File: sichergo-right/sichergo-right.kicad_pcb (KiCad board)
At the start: 2 copper layers, 173 parts, among them J1 Conn_01x04_Pin, J2 Conn_01x04_Pin, Q1 2N7002, Q2 2N7002, SW1 SW_Push, SW10 SW_Push, SW11 SW_Push, SW12 SW_Push, SW13 SW_Push, SW14 SW_Push, SW15 SW_Push, SW16 SW_Push, SW17 SW_Push, SW18 SW_Push, SW19 SW_Push, SW20 SW_Push, SW21 SW_Push, SW22 SW_Push, SW23 SW_Push, SW24 SW_Push, SW25 SW_Push, SW26 SW_Push, SW27 SW_Push, SW28 SW_Push, SW29 SW_Push, SW3 SW_Push, SW30 SW_Push, SW31 SW_Push, SW32 SW_Push, SW33 SW_Push, SW34 SW_Push, SW35 SW_Push, SW36 SW_Push, SW37 SW_Push, SW4 SW_Push, SW5 SW_Push, SW6 SW_Push, SW7 SW_Push, SW8 SW_Push, SW9 SW_Push, U1 AZ1117-3.3, U10 SN74LVC1G125DBV, U2 TPD4E05U06DQA, U3 YTS1C0033BBG01, U4 STM32F103C8Tx, U5 SN74LVC1G125DBV, U6 SN74LVC1G125DBV, U7 YTS1C0033BBG01, U8 STM32F103C8Tx, U9 SN74LVC1G125DBV, Y1 Crystal_GND24, Y2 Crystal_GND24

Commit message: Split design in two PCBs and remake layout
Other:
- board outline added: 268.1 x 155.2 mm

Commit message: Remake entire shape
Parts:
- removed Audio2: PJ-327E-SMT, easyeda2kicad:AUDIO-SMD_PJ-327E-SMT
- removed D38, D39, D40, D41, D42, D43, D44, D45, D46, D47, D48, D49, D50, D51, D52, D53, D54, D55, D56, D57, D58, D59, D60, D61, D62, D63, D64, D65, D66, D67, D68, D69, D70, D71, D72, D73: LED, LED_SMD:LED_0603_1608Metric_Pad1.05x0.95mm_HandSolder
- removed J2: Conn_01x04_Pin, Connector_PinSocket_2.54mm:PinSocket_1x04_P2.54mm_Horizontal
- removed Q2: 2N7002, Package_TO_SOT_SMD:SOT-23_Handsoldering
- removed R29, R30, R32, R33, R34, R35, R36, R37, R38, R39, R40, R41, R42, R43, R44, R45, R46, R47, R48, R49, R50: 1 kohm, Resistor_SMD:R_0603_1608Metric_Pad0.98x0.95mm_HandSolder
- removed R51, R52: 5.1 kohm, Resistor_SMD:R_0612_1632Metric_Pad1.18x3.40mm_HandSolder
- removed SW20, SW21, SW22, SW23, SW24, SW25, SW26, SW27, SW28, SW29, SW30, SW31, SW32, SW33, SW34, SW35, SW36, SW37: SW_Push, personal:Gateron_Milky_Yellow
- removed U10, U9: SN74LVC1G125DBV, Package_TO_SOT_SMD:SOT-23-5_HandSoldering
- removed U7: YTS1C0033BBG01, easyeda2kicad:SW-SMD_YIYUAN_YTS1C003XXX
- removed U8: STM32F103C8Tx, Package_QFP:LQFP-48_7x7mm_P0.5mm
- removed Y2: Crystal_GND24, Crystal:Crystal_SMD_3225-4Pin_3.2x2.5mm_HandSoldering
- added C1: 10 µF, Capacitor_SMD:C_0805_2012Metric_Pad1.18x1.45mm_HandSolder, F.Cu at (138.7, 36.0)
- added C10: 10 µF, Capacitor_SMD:C_0805_2012Metric_Pad1.18x1.45mm_HandSolder, F.Cu at (193.1, 12.2)
- added C11: 0.1 µF, Capacitor_SMD:C_0805_2012Metric_Pad1.18x1.45mm_HandSolder, F.Cu at (168.4, 20.8)
- added C12: 1 µF, Capacitor_SMD:C_0805_2012Metric_Pad1.18x1.45mm_HandSolder, F.Cu at (164.8, 20.8)
- added C13: 10000 pF, Capacitor_SMD:C_0805_2012Metric_Pad1.18x1.45mm_HandSolder, F.Cu at (133.0, 25.6)
- added C2: 22 µF, Capacitor_SMD:C_0805_2012Metric_Pad1.18x1.45mm_HandSolder, F.Cu at (115.0, 20.8)
- added C3: 10 pF, Capacitor_SMD:C_0805_2012Metric_Pad1.18x1.45mm_HandSolder, F.Cu at (173.4, 26.4)
- added C4: 10 pF, Capacitor_SMD:C_0805_2012Metric_Pad1.18x1.45mm_HandSolder, F.Cu at (170.4, 20.8)
- added C5: 0.1 µF, Capacitor_SMD:C_0805_2012Metric_Pad1.18x1.45mm_HandSolder, F.Cu at (162.8, 20.8)
- added C6: 0.1 µF, Capacitor_SMD:C_0805_2012Metric_Pad1.18x1.45mm_HandSolder, F.Cu at (165.3, 29.5)
- added C7: 0.1 µF, Capacitor_SMD:C_0805_2012Metric_Pad1.18x1.45mm_HandSolder, F.Cu at (151.5, 20.1)
- added C8: 0.1 µF, Capacitor_SMD:C_0805_2012Metric_Pad1.18x1.45mm_HandSolder, F.Cu at (148.4, 36.4)
- added C9: 0.1 µF, Capacitor_SMD:C_0805_2012Metric_Pad1.18x1.45mm_HandSolder, F.Cu at (193.1, 10.1)
- added L1: 120 Ohm @ 100 MHz, Inductor_SMD:L_0603_1608Metric_Pad1.05x0.95mm_HandSolder, F.Cu at (122.9, 19.5)
- added R10: 1 kohm, Resistor_SMD:R_0603_1608Metric_Pad0.98x0.95mm_HandSolder, F.Cu at (98.5, 88.6)
- added R11: 1 kohm, Resistor_SMD:R_0603_1608Metric_Pad0.98x0.95mm_HandSolder, F.Cu at (98.6, 108.1)
- added R12: 1 kohm, Resistor_SMD:R_0603_1608Metric_Pad0.98x0.95mm_HandSolder, F.Cu at (95.0, 67.0)
- added R3: 4.7 kohm, Resistor_SMD:R_0603_1608Metric_Pad0.98x0.95mm_HandSolder, F.Cu at (133.5, 20.9)
- added R4: 4.7 kohm, Resistor_SMD:R_0603_1608Metric_Pad0.98x0.95mm_HandSolder, F.Cu at (200.2, 52.5)
- added R5: 4.7 kohm, Resistor_SMD:R_0603_1608Metric_Pad0.98x0.95mm_HandSolder, F.Cu at (207.0, 51.9)
- added R6: 4.7 kohm, Resistor_SMD:R_0603_1608Metric_Pad0.98x0.95mm_HandSolder, F.Cu at (165.5, 49.3)
- added R9: 100 ohm, Resistor_SMD:R_0603_1608Metric_Pad0.98x0.95mm_HandSolder, F.Cu at (197.9, 17.1)
- added SW2: SW_Push, personal:Gateron_Milky_Yellow, F.Cu at (100.3, 78.9)
- added TP1: TestPoint, TestPoint:TestPoint_THTPad_1.0x1.0mm_Drill0.5mm, F.Cu at (116.0, 18.5)
- added TP3: TestPoint, TestPoint:TestPoint_THTPad_1.0x1.0mm_Drill0.5mm, F.Cu at (119.4, 25.4)
- added TP4: TestPoint, TestPoint:TestPoint_THTPad_1.0x1.0mm_Drill0.5mm, F.Cu at (105.9, 28.5)
- added TP7: TestPoint, TestPoint:TestPoint_THTPad_1.0x1.0mm_Drill0.5mm, F.Cu at (93.5, 33.0)
- added TP8: TestPoint, TestPoint:TestPoint_THTPad_1.0x1.0mm_Drill0.5mm, F.Cu at (200.2, 11.3)
- added TP9: TestPoint, TestPoint:TestPoint_THTPad_1.0x1.0mm_Drill0.5mm, F.Cu at (197.8, 11.2)
- D10, D14, D15, D16, D17, D2, D22, D23, D24, D25, D3, D30, D31, D32, D33, D4, D8, D9: value CD4148W -> LED; footprint Diode_SMD:D_0805_2012Metric_Pad1.15x1.40mm_HandSolder -> LED_SMD:LED_0603_1608Metric_Pad1.05x0.95mm_HandSolder
- R13: value 5.1 kohm -> 1 kohm
- R14: value 100 ohm -> 1 kohm; footprint Resistor_SMD:R_0805_2012Metric_Pad1.20x1.40mm_HandSolder -> Resistor_SMD:R_0603_1608Metric_Pad0.98x0.95mm_HandSolder
- R2, R8: value 4.7 kohm -> 5.1 kohm
- R28: value 1 kohm -> 4.7 kohm
- R31: value 1 kohm -> 1.5 kohm
- R7: value 100 ohm -> 4.7 kohm; footprint Resistor_SMD:R_0805_2012Metric_Pad1.20x1.40mm_HandSolder -> Resistor_SMD:R_0603_1608Metric_Pad0.98x0.95mm_HandSolder
- SW19: value SW_Push -> MS-22C01-G010; footprint personal:Gateron_Milky_Yellow -> easyeda2kicad:SW-SMD_6P-L7.2-W3.5-P2.50-LS6.0-TL
- moved D21 253.1 mm to (137.0, 126.8), turned to 90 degrees
- moved D17 253.0 mm to (129.9, 127.7), turned to 180 degrees
- moved D37 251.1 mm to (180.0, 132.7), turned to 90 degrees
- moved D29 249.9 mm to (157.5, 130.2), turned to 90 degrees
- moved D3 249.6 mm to (102.3, 108.1), turned to 180 degrees
- moved D10 243.9 mm to (116.9, 106.0), turned to 180 degrees
- moved D16 243.3 mm to (132.1, 105.9), turned to 180 degrees
- moved D33 241.3 mm to (170.9, 132.5), turned to 150 degrees
- moved D25 240.7 mm to (149.1, 130.4), turned to 165 degrees
- moved D20 236.1 mm to (136.3, 105.8), turned to 90 degrees
- moved D2 234.5 mm to (102.1, 88.6), turned to 180 degrees
- moved D13 233.8 mm to (121.0, 105.8), turned to 90 degrees
- moved D7 230.3 mm to (109.9, 102.6), turned to 90 degrees
- moved D28 229.5 mm to (151.2, 107.1), turned to 90 degrees
- moved D9 229.0 mm to (117.0, 86.9), turned to 180 degrees
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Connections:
- D1 pad 2: /KBD_L/VBUS -> (no net)
- D10 pad 1: /KBD_L/KB_ROW_1 -> GND
- D11 pad 1: /KBD_L/KB_ROW_1 -> (no net)
- D12 pad 1: /KBD_L/KB_ROW_2 -> (no net)
- D13 pad 1: /KBD_L/KB_ROW_2 -> (no net)
- D14 pad 1: /KBD_L/KB_ROW_2 -> GND
- D15 pad 1: /KBD_L/KB_ROW_2 -> GND
- D16 pad 1: /KBD_L/KB_ROW_2 -> GND
- D17 pad 1: /KBD_R/KB_ROW_4 -> GND
- D18 pad 1: /KBD_R/KB_ROW_5 -> (no net)
- D19 pad 1: /KBD_L/KB_ROW_3 -> (no net)
- D2 pad 1: /KBD_L/KB_ROW_0 -> GND
- D20 pad 1: /KBD_L/KB_ROW_3 -> (no net)
- D21 pad 1: /KBD_L/KB_ROW_3 -> (no net)
- D22 pad 1: /KBD_R/KB_ROW_6 -> GND
- D23 pad 1: /KBD_R/KB_ROW_4 -> GND
- D24 pad 1: /KBD_R/KB_ROW_5 -> GND
- D25 pad 1: /KBD_R/KB_ROW_6 -> GND
- D26 pad 1: /KBD_R/KB_ROW_4 -> (no net)
- D27 pad 1: /KBD_R/KB_ROW_5 -> (no net)
- D28 pad 1: /KBD_R/KB_ROW_6 -> (no net)
- D29 pad 1: /KBD_R/KB_ROW_7 -> (no net)
- D3 pad 1: /KBD_L/KB_ROW_0 -> GND
- D30 pad 1: /KBD_R/KB_ROW_4 -> GND
- D31 pad 1: /KBD_R/KB_ROW_5 -> GND
- D32 pad 1: /KBD_R/KB_ROW_6 -> GND
- D33 pad 1: /KBD_R/KB_ROW_7 -> GND
- D34 pad 1: /KBD_R/KB_ROW_4 -> (no net)
- D35 pad 1: /KBD_R/KB_ROW_5 -> (no net)
- D36 pad 1: /KBD_R/KB_ROW_6 -> (no net)
- D37 pad 1: /KBD_R/KB_ROW_7 -> (no net)
- D4 pad 1: /KBD_L/KB_ROW_0 -> GND
- D5 pad 1: /KBD_L/KB_ROW_0 -> (no net)
- D6 pad 1: /KBD_L/KB_ROW_0 -> (no net)
- D7 pad 1: /KBD_L/KB_ROW_1 -> (no net)
- D8 pad 1: /KBD_L/KB_ROW_1 -> GND
- D9 pad 1: /KBD_L/KB_ROW_1 -> GND
- F1 pad 1: /KBD_L/VBUS -> (no net)
- Q1 pad 3: +3V3 -> (no net)
- R1 pad 1: Net-(USB1-CC1) -> Net-(USB1-CC2)
- R13 pad 1: Net-(USB1-CC2) -> (no net)
- R13 pad 2: GND -> Net-(D8-A)
- R14 pad 1: Net-(Audio2-Pad1) -> (no net)
- R14 pad 2: GND -> Net-(D9-A)
- R15 pad 1: +3V3 -> (no net)
- R15 pad 2: Net-(D38-A) -> Net-(D10-A)
- R16 pad 1: +3V3 -> (no net)
- R16 pad 2: Net-(D39-A) -> Net-(D14-A)
- R17 pad 1: +3V3 -> (no net)
- R17 pad 2: Net-(D40-A) -> Net-(D15-A)
- R18 pad 1: +3V3 -> (no net)
- R18 pad 2: Net-(D44-A) -> Net-(D16-A)
- R19 pad 1: +3V3 -> (no net)
- R19 pad 2: Net-(D45-A) -> Net-(D17-A)
- R2 pad 1: +3V3 -> Net-(USB1-CC1)
- R2 pad 2: Net-(U4-NRST) -> GND
- R20 pad 1: +3V3 -> (no net)
- R20 pad 2: Net-(D43-A) -> Net-(D22-A)
- R21 pad 1: +3V3 -> (no net)
- R21 pad 2: Net-(D48-A) -> Net-(D23-A)
- R22 pad 1: +3V3 -> (no net)
- R22 pad 2: Net-(D42-A) -> Net-(D24-A)
- R23 pad 1: +3V3 -> (no net)
- R23 pad 2: Net-(D41-A) -> Net-(D25-A)
- R24 pad 1: +3V3 -> (no net)
- R24 pad 2: Net-(D51-A) -> Net-(D30-A)
- R25 pad 1: +3V3 -> (no net)
- R25 pad 2: Net-(D50-A) -> Net-(D31-A)
- R26 pad 1: +3V3 -> (no net)
- R26 pad 2: Net-(D49-A) -> Net-(D32-A)
- R27 pad 1: +3V3 -> (no net)
- R27 pad 2: Net-(D46-A) -> Net-(D33-A)
- R28 pad 1: +3V3 -> (no net)
- R28 pad 2: Net-(D47-A) -> +3V3
- R31 pad 2: Net-(D53-A) -> (no net)
- R7 pad 1: Net-(Audio1-Pad1) -> Net-(U4-BOOT0)
- R8 pad 1: +3V3 -> Net-(Q1-G)
- R8 pad 2: Net-(U8-NRST) -> GND
- SW1 pad 1: /KBD_L/KB_COL_0 -> (no net)
- SW1 pad 2: Net-(D2-A) -> Net-(D5-A)
- SW10 pad 1: /KBD_L/KB_COL_3 -> (no net)
- SW10 pad 2: Net-(D10-A) -> Net-(D21-A)
- SW11 pad 1: /KBD_L/KB_COL_4 -> (no net)
- SW11 pad 2: Net-(D11-A) -> Net-(D26-A)
- SW12 pad 1: /KBD_L/KB_COL_0 -> (no net)
- SW12 pad 2: Net-(D12-A) -> Net-(D27-A)
- SW13 pad 1: /KBD_L/KB_COL_1 -> (no net)
- SW13 pad 2: Net-(D13-A) -> Net-(D28-A)
- SW14 pad 1: /KBD_L/KB_COL_2 -> (no net)
- SW14 pad 2: Net-(D14-A) -> Net-(D29-A)
- SW15 pad 1: /KBD_L/KB_COL_3 -> (no net)
- SW15 pad 2: Net-(D15-A) -> Net-(D34-A)
- SW16 pad 1: /KBD_L/KB_COL_4 -> (no net)
- SW16 pad 2: Net-(D16-A) -> Net-(D35-A)
- SW17 pad 1: /KBD_R/KB_COL_0 -> (no net)
- SW17 pad 2: Net-(D17-A) -> Net-(D36-A)
- SW18 pad 1: /KBD_R/KB_COL_0 -> (no net)
- SW18 pad 2: Net-(D18-A) -> Net-(D37-A)
- SW19 pad 1: /KBD_L/KB_COL_2 -> (no net)
- SW19 pad 2: Net-(D19-A) -> Net-(J1-Pin_3)
- SW3 pad 1: /KBD_L/KB_COL_1 -> (no net)
- SW3 pad 2: Net-(D3-A) -> Net-(D7-A)
- SW4 pad 1: /KBD_L/KB_COL_2 -> (no net)
- SW4 pad 2: Net-(D4-A) -> Net-(D11-A)
- SW5 pad 1: /KBD_L/KB_COL_3 -> (no net)
- SW5 pad 2: Net-(D5-A) -> Net-(D12-A)
- SW6 pad 1: /KBD_L/KB_COL_4 -> (no net)
- SW6 pad 2: Net-(D6-A) -> Net-(D13-A)
- SW7 pad 1: /KBD_L/KB_COL_0 -> (no net)
- SW7 pad 2: Net-(D7-A) -> Net-(D18-A)
- SW8 pad 1: /KBD_L/KB_COL_1 -> (no net)
- SW8 pad 2: Net-(D8-A) -> Net-(D19-A)
- SW9 pad 1: /KBD_L/KB_COL_2 -> (no net)
- SW9 pad 2: Net-(D9-A) -> Net-(D20-A)
- U2 pad 1: /KBD_L/D+ -> (no net)
- U2 pad 2: /KBD_L/D- -> (no net)
- U4 pad 10: /KBD_L/KB_COL_0 -> (no net)
- U4 pad 11: /KBD_L/KB_COL_1 -> (no net)
- U4 pad 12: /KBD_L/KB_COL_2 -> (no net)
- U4 pad 13: /KBD_L/KB_COL_3 -> (no net)
- U4 pad 14: /KBD_L/KB_COL_4 -> (no net)
- U4 pad 15: /KBD_L/KB_ROW_0 -> (no net)
- U4 pad 16: /KBD_L/KB_ROW_1 -> (no net)
- U4 pad 17: /KBD_L/KB_ROW_2 -> (no net)
- U4 pad 26: Net-(Q2-G) -> Net-(Q1-G)
- U4 pad 29: /KBD_L/KB_ROW_3 -> (no net)
- U4 pad 30: /KBD_L/UART_TX -> (no net)
- U4 pad 31: /KBD_L/UART_RX -> (no net)
- U4 pad 32: unconnected-(U4-PA11-Pad32) -> (no net)
- U4 pad 33: unconnected-(U4-PA12-Pad33) -> (no net)
- U4 pad 34: /KBD_L/SWDIO -> (no net)
- U4 pad 37: /KBD_L/SWCLK -> (no net)
- U4 pad 38: unconnected-(U4-PA15-Pad38) -> (no net)
- U4 pad 39: unconnected-(U4-PB3-Pad39) -> (no net)
- U4 pad 40: unconnected-(U4-PB4-Pad40) -> (no net)
- U4 pad 41: unconnected-(U4-PB5-Pad41) -> (no net)
- U4 pad 42: /KBD_L/OLED_SCL -> (no net)
- U4 pad 43: /KBD_L/OLED_SDA -> (no net)
- U5 pad 2: /KBD_L/UART_TX -> Net-(Audio1-Pad4)
- U5 pad 4: Net-(Audio1-Pad3) -> (no net)
- U6 pad 2: Net-(Audio1-Pad4) -> (no net)
- U6 pad 4: /KBD_L/UART_RX -> Net-(Audio1-Pad3)
- USB1 pad 11: /KBD_L/VBUS -> (no net)
- USB1 pad 13: GND -> (no net)
- USB1 pad 14: GND -> (no net)
- USB1 pad 2: /KBD_L/VBUS -> (no net)
- USB1 pad 5: /KBD_L/D- -> (no net)
- USB1 pad 6: /KBD_L/D+ -> (no net)
- USB1 pad 7: /KBD_L/D- -> (no net)
- USB1 pad 8: /KBD_L/D+ -> (no net)
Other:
- board outline removed
- board text added: "Daniel (steewBSD)"
- board text added: "NP"

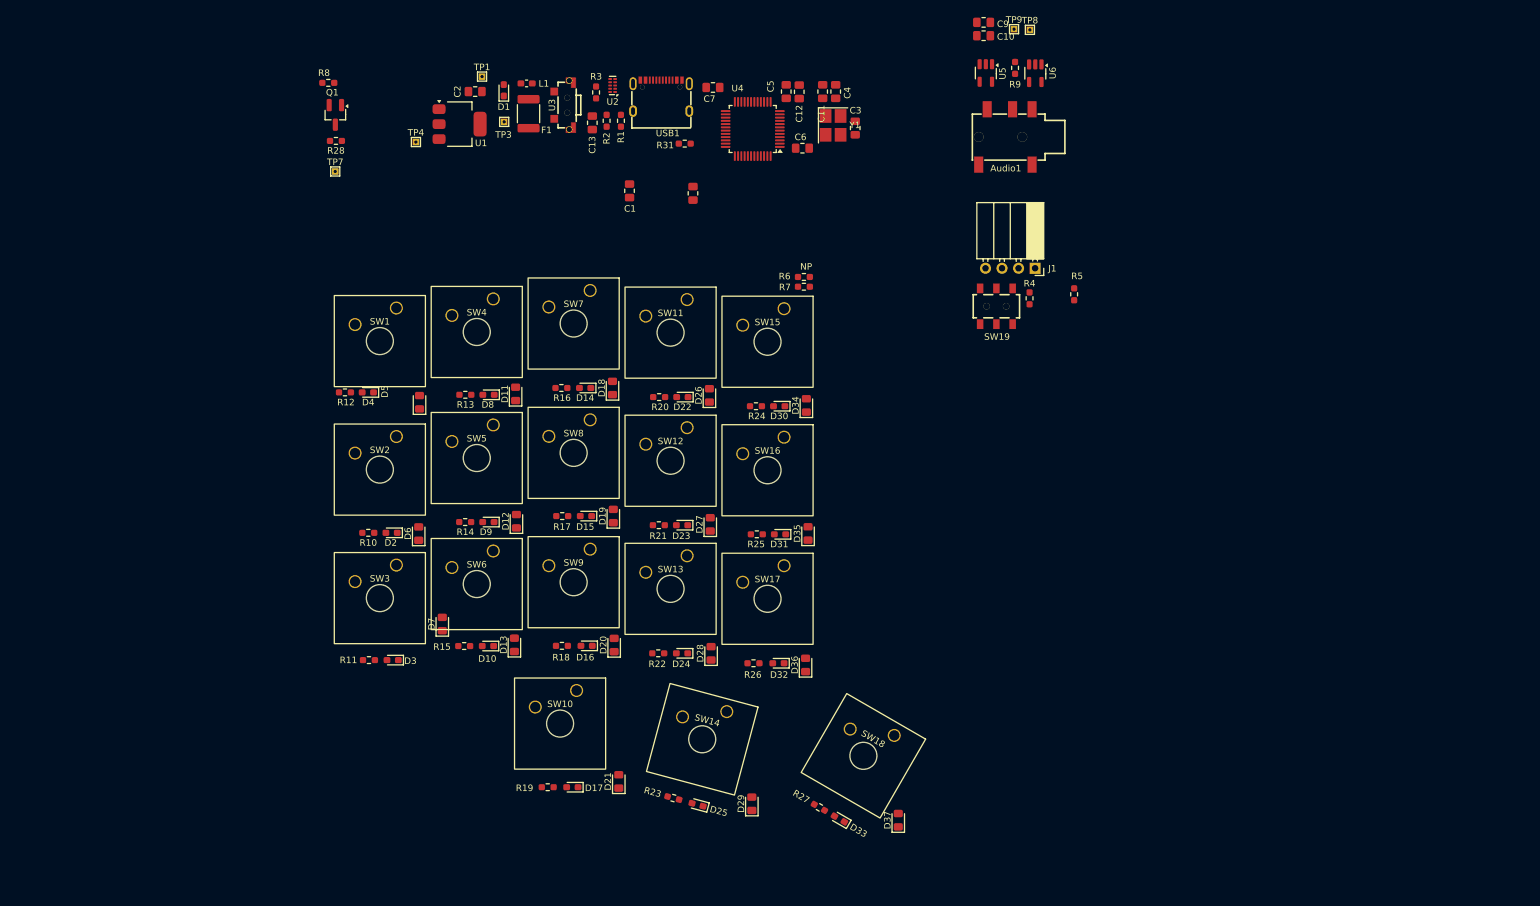
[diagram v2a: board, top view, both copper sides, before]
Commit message: Fix keyboard layout size
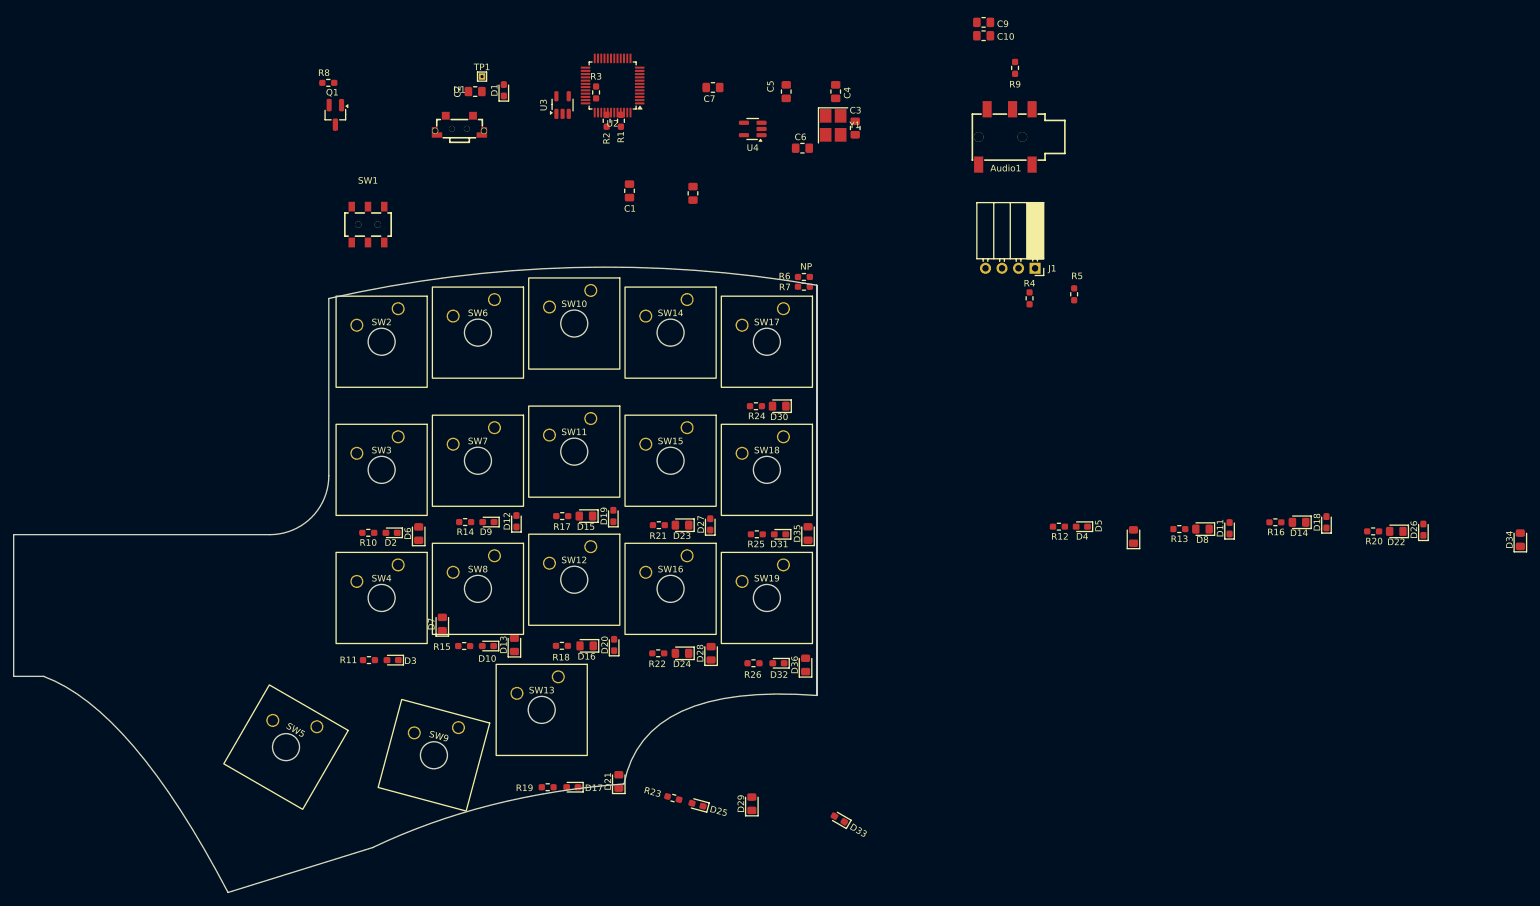
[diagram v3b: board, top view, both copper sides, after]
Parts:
- removed C11: 0.1 µF, Capacitor_SMD:C_0805_2012Metric_Pad1.18x1.45mm_HandSolder
- removed C12: 1 µF, Capacitor_SMD:C_0805_2012Metric_Pad1.18x1.45mm_HandSolder
- removed C13: 10000 pF, Capacitor_SMD:C_0805_2012Metric_Pad1.18x1.45mm_HandSolder
- removed D37: CD4148W, Diode_SMD:D_0805_2012Metric_Pad1.15x1.40mm_HandSolder
- removed F1: 1812L050/30PR, Fuse:Fuse_1812_4532Metric_Pad1.30x3.40mm_HandSolder
- removed L1: 120 Ohm @ 100 MHz, Inductor_SMD:L_0603_1608Metric_Pad1.05x0.95mm_HandSolder
- removed R27: 1 kohm, Resistor_SMD:R_0603_1608Metric_Pad0.98x0.95mm_HandSolder
- removed R28: 4.7 kohm, Resistor_SMD:R_0603_1608Metric_Pad0.98x0.95mm_HandSolder
- removed R31: 1.5 kohm, Resistor_SMD:R_0603_1608Metric_Pad0.98x0.95mm_HandSolder
- removed TP3, TP4, TP7, TP8, TP9: TestPoint, TestPoint:TestPoint_THTPad_1.0x1.0mm_Drill0.5mm
- removed U5, U6: SN74LVC1G125DBV, Package_TO_SOT_SMD:SOT-23-5_HandSoldering
- removed USB1: TYPE-C 16PIN 2MD(073), easyeda2kicad:USB-C-SMD_TYPE-C-6PIN-2MD-073
- C1: value 10 µF -> 10 pF
- C10: value 10 µF -> 1 µF
- C2: value 22 µF -> 10 pF
- C3, C4: value 10 pF -> 0.1 µF
- C8: value 0.1 µF -> 10 µF
- D1: value CPDUR5V0HE-HF -> LED; footprint Diode_SMD:D_0603_1608Metric_Pad1.05x0.95mm_HandSolder -> LED_SMD:LED_0603_1608Metric_Pad1.05x0.95mm_HandSolder
- D11, D12, D18, D19, D20, D26, D27: value CD4148W -> LED; footprint Diode_SMD:D_0805_2012Metric_Pad1.15x1.40mm_HandSolder -> LED_SMD:LED_0603_1608Metric_Pad1.05x0.95mm_HandSolder
- D14, D15, D16, D22, D23, D24, D30, D8: value LED -> CD4148W; footprint LED_SMD:LED_0603_1608Metric_Pad1.05x0.95mm_HandSolder -> Diode_SMD:D_0805_2012Metric_Pad1.15x1.40mm_HandSolder
- R1, R2: value 5.1 kohm -> 4.7 kohm
- R7: value 4.7 kohm -> 5.1 kohm
- R8: value 5.1 kohm -> 100 ohm
- R9: value 100 ohm -> 1 kohm
- SW1: value SW_Push -> MS-22C01-G010; footprint personal:Gateron_Milky_Yellow -> easyeda2kicad:SW-SMD_6P-L7.2-W3.5-P2.50-LS6.0-TL
- SW19: value MS-22C01-G010 -> SW_Push; footprint easyeda2kicad:SW-SMD_6P-L7.2-W3.5-P2.50-LS6.0-TL -> personal:Gateron_Milky_Yellow
- U1: value AZ1117-3.3 -> YTS1C0033BBG01; footprint Package_TO_SOT_SMD:SOT-223-3_TabPin2 -> easyeda2kicad:SW-SMD_YIYUAN_YTS1C003XXX
- U2: value TPD4E05U06DQA -> STM32F103C8Tx; footprint Package_SON:USON-10_2.5x1.0mm_P0.5mm -> Package_QFP:LQFP-48_7x7mm_P0.5mm
- U3: value YTS1C0033BBG01 -> SN74LVC1G125DBV; footprint easyeda2kicad:SW-SMD_YIYUAN_YTS1C003XXX -> Package_TO_SOT_SMD:SOT-23-5_HandSoldering
- U4: value STM32F103C8Tx -> SN74LVC1G125DBV; footprint Package_QFP:LQFP-48_7x7mm_P0.5mm -> Package_TO_SOT_SMD:SOT-23-5_HandSoldering
- moved D8 111.6 mm to (226.7, 88.0)
- moved R12 111.6 mm to (204.7, 87.6)
- moved D11 111.6 mm to (230.9, 87.9)
- moved D14 111.6 mm to (241.6, 87.0)
- moved D18 111.6 mm to (245.8, 87.0)
- moved D26 111.6 mm to (260.7, 88.1)
- moved D34 111.6 mm to (275.6, 89.6)
- moved D4 111.6 mm to (208.2, 87.6)
- moved D5 111.6 mm to (216.1, 89.1)
- moved R13 111.6 mm to (223.2, 88.0)
- moved R16 111.6 mm to (237.9, 87.0)
- moved R20 111.6 mm to (253.0, 88.4)
- moved D22 111.6 mm to (256.5, 88.4)
- moved SW14 62.7 mm to (145.0, 57.8), turned to 0 degrees
- moved SW10 61.5 mm to (130.2, 56.4)
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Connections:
- C1 pad 1: (no net) -> Net-(U2-PD0)
- C2 pad 1: +3V3 -> Net-(U2-PD1)
- C3 pad 1: Net-(U4-PD0) -> Net-(U2-NRST)
- C4 pad 1: Net-(U4-PD1) -> +3V3
- C5 pad 1: Net-(U4-NRST) -> +3V3
- D1 pad 2: (no net) -> Net-(D1-A)
- D11 pad 1: (no net) -> GND
- D12 pad 1: (no net) -> GND
- D13 pad 1: (no net) -> /KB_ROW_0
- D14 pad 1: GND -> /KB_ROW_1
- D15 pad 1: GND -> /KB_ROW_2
- D16 pad 1: GND -> /KB_ROW_3
- D18 pad 1: (no net) -> GND
- D19 pad 1: (no net) -> GND
- D20 pad 1: (no net) -> GND
- D21 pad 1: (no net) -> /KB_ROW_0
- D22 pad 1: GND -> /KB_ROW_1
- D23 pad 1: GND -> /KB_ROW_2
- D24 pad 1: GND -> /KB_ROW_3
- D26 pad 1: (no net) -> GND
- D27 pad 1: (no net) -> GND
- D28 pad 1: (no net) -> /KB_ROW_0
- D29 pad 1: (no net) -> /KB_ROW_1
- D30 pad 1: GND -> /KB_ROW_2
- D34 pad 1: (no net) -> /KB_ROW_0
- D35 pad 1: (no net) -> /KB_ROW_1
- D36 pad 1: (no net) -> /KB_ROW_2
- D5 pad 1: (no net) -> /KB_ROW_0
- D6 pad 1: (no net) -> /KB_ROW_1
- D7 pad 1: (no net) -> /KB_ROW_2
- D8 pad 1: GND -> /KB_ROW_3
- Q1 pad 3: (no net) -> /MatrixR/LED_DRIVE
- R1 pad 1: Net-(USB1-CC2) -> +3V3
- R1 pad 2: GND -> /OLED_SCL
- R10 pad 1: (no net) -> /MatrixR/LED_DRIVE
- R11 pad 1: (no net) -> /MatrixR/LED_DRIVE
- R12 pad 1: (no net) -> /MatrixR/LED_DRIVE
- R13 pad 1: (no net) -> /MatrixR/LED_DRIVE
- R13 pad 2: Net-(D8-A) -> Net-(D9-A)
- R14 pad 1: (no net) -> /MatrixR/LED_DRIVE
- R14 pad 2: Net-(D9-A) -> Net-(D10-A)
- R15 pad 1: (no net) -> /MatrixR/LED_DRIVE
- R15 pad 2: Net-(D10-A) -> Net-(D11-A)
- R16 pad 1: (no net) -> /MatrixR/LED_DRIVE
- R16 pad 2: Net-(D14-A) -> Net-(D12-A)
- R17 pad 1: (no net) -> /MatrixR/LED_DRIVE
- R17 pad 2: Net-(D15-A) -> Net-(D17-A)
- R18 pad 1: (no net) -> /MatrixR/LED_DRIVE
- R18 pad 2: Net-(D16-A) -> Net-(D18-A)
- R19 pad 1: (no net) -> /MatrixR/LED_DRIVE
- R19 pad 2: Net-(D17-A) -> Net-(D19-A)
- R2 pad 1: Net-(USB1-CC1) -> +3V3
- R2 pad 2: GND -> Net-(U2-NRST)
- R20 pad 1: (no net) -> /MatrixR/LED_DRIVE
- R20 pad 2: Net-(D22-A) -> Net-(D20-A)
- R21 pad 1: (no net) -> /MatrixR/LED_DRIVE
- R21 pad 2: Net-(D23-A) -> Net-(D25-A)
- R22 pad 1: (no net) -> /MatrixR/LED_DRIVE
- R22 pad 2: Net-(D24-A) -> Net-(D26-A)
- R23 pad 1: (no net) -> /MatrixR/LED_DRIVE
- R23 pad 2: Net-(D25-A) -> Net-(D27-A)
- R24 pad 1: (no net) -> /MatrixR/LED_DRIVE
- R24 pad 2: Net-(D30-A) -> Net-(D31-A)
- R25 pad 1: (no net) -> /MatrixR/LED_DRIVE
- R25 pad 2: Net-(D31-A) -> Net-(D32-A)
- R26 pad 1: (no net) -> /MatrixR/LED_DRIVE
- R26 pad 2: Net-(D32-A) -> Net-(D33-A)
- R3 pad 2: Net-(U4-NRST) -> /OLED_SDA
- R4 pad 2: (no net) -> /MatrixR/LED_DRIVE
- R5 pad 2: (no net) -> Net-(U2-BOOT0)
- R6 pad 1: +3V3 -> Net-(U2-BOOT0)
- R6 pad 2: Net-(U4-BOOT0) -> GND
- R7 pad 1: Net-(U4-BOOT0) -> Net-(Q1-G)
- R8 pad 1: Net-(Q1-G) -> GND
- R8 pad 2: GND -> Net-(Audio1-Pad1)
- R9 pad 1: GND -> /MatrixR/LED_DRIVE
- R9 pad 2: Net-(Audio1-Pad1) -> Net-(D1-A)
- SW1 pad 1: (no net) -> /SWCLK
- SW1 pad 2: Net-(D5-A) -> Net-(J1-Pin_3)
- SW10 pad 1: (no net) -> /KB_COL_2
- SW11 pad 1: (no net) -> /KB_COL_2
- SW11 pad 2: Net-(D26-A) -> Net-(D22-A)
- SW12 pad 1: (no net) -> /KB_COL_2
- SW12 pad 2: Net-(D27-A) -> Net-(D23-A)
- SW13 pad 1: (no net) -> /KB_COL_2
- SW13 pad 2: Net-(D28-A) -> Net-(D24-A)
- SW14 pad 1: (no net) -> /KB_COL_3
- SW14 pad 2: Net-(D29-A) -> Net-(D28-A)
- SW15 pad 1: (no net) -> /KB_COL_3
- SW15 pad 2: Net-(D34-A) -> Net-(D29-A)
- SW16 pad 1: (no net) -> /KB_COL_3
- SW16 pad 2: Net-(D35-A) -> Net-(D30-A)
- SW17 pad 1: (no net) -> /KB_COL_4
- SW17 pad 2: Net-(D36-A) -> Net-(D34-A)
- SW18 pad 1: (no net) -> /KB_COL_4
- SW18 pad 2: Net-(D37-A) -> Net-(D35-A)
- SW19 pad 1: (no net) -> /KB_COL_4
- SW19 pad 2: Net-(J1-Pin_3) -> Net-(D36-A)
- SW2 pad 1: (no net) -> /KB_COL_0
- SW2 pad 2: Net-(D6-A) -> Net-(D5-A)
- SW3 pad 1: (no net) -> /KB_COL_0
- SW3 pad 2: Net-(D7-A) -> Net-(D6-A)
- SW4 pad 1: (no net) -> /KB_COL_0
- SW4 pad 2: Net-(D11-A) -> Net-(D7-A)
- SW5 pad 1: (no net) -> /KB_COL_0
- SW5 pad 2: Net-(D12-A) -> Net-(D8-A)
- SW6 pad 1: (no net) -> /KB_COL_1
- SW7 pad 1: (no net) -> /KB_COL_1
- SW7 pad 2: Net-(D18-A) -> Net-(D14-A)
- SW8 pad 1: (no net) -> /KB_COL_1
- SW8 pad 2: Net-(D19-A) -> Net-(D15-A)
- SW9 pad 1: (no net) -> /KB_COL_1
- SW9 pad 2: Net-(D20-A) -> Net-(D16-A)
- TP1 pad 1: +3V3 -> /MatrixR/LED_DRIVE
- U1 pad 2: +3V3 -> Net-(U2-NRST)
- U1 pad 3: Net-(U1-VI) -> GND
- U2 pad 1: (no net) -> +3V3
- U2 pad 2: (no net) -> unconnected-(U2-PC13-Pad2)
- U2 pad 3: GND -> unconnected-(U2-PC14-Pad3)
- U2 pad 5: unconnected-(U2-D2--Pad5) -> Net-(U2-PD0)
- U2 pad 6: unconnected-(U2-NC-Pad6) -> Net-(U2-PD1)
- U2 pad 7: unconnected-(U2-NC-Pad7) -> Net-(U2-NRST)
- U2 pad 9: unconnected-(U2-NC-Pad9) -> +3V3
- U3 pad 2: Net-(U4-NRST) -> Net-(Audio1-Pad3)
- U3 pad 4: GND -> /UART_RX
- U4 pad 1: +3V3 -> GND
- U4 pad 2: unconnected-(U4-PC13-Pad2) -> /UART_TX
- U4 pad 3: unconnected-(U4-PC14-Pad3) -> GND
- U4 pad 4: unconnected-(U4-PC15-Pad4) -> Net-(Audio1-Pad4)
- U4 pad 5: Net-(U4-PD0) -> +3V3
- Y1 pad 1: Net-(U4-PD1) -> Net-(U2-PD1)
- Y1 pad 3: Net-(U4-PD0) -> Net-(U2-PD0)
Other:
- board outline added: 123.4 x 96.1 mm
